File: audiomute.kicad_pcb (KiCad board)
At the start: 2 copper layers, 72.8 x 35.4 mm, 21 parts, among them J1 MJ-3523-SMT, J2 B2B-XH-A_LF__SN_, J3 B2B-XH-A_LF__SN_, J4 MJ-3523-SMT, Q1 MMBT3904, Q2 MMBT3906, Q3 MMBT3904, Q4 MMBT3904

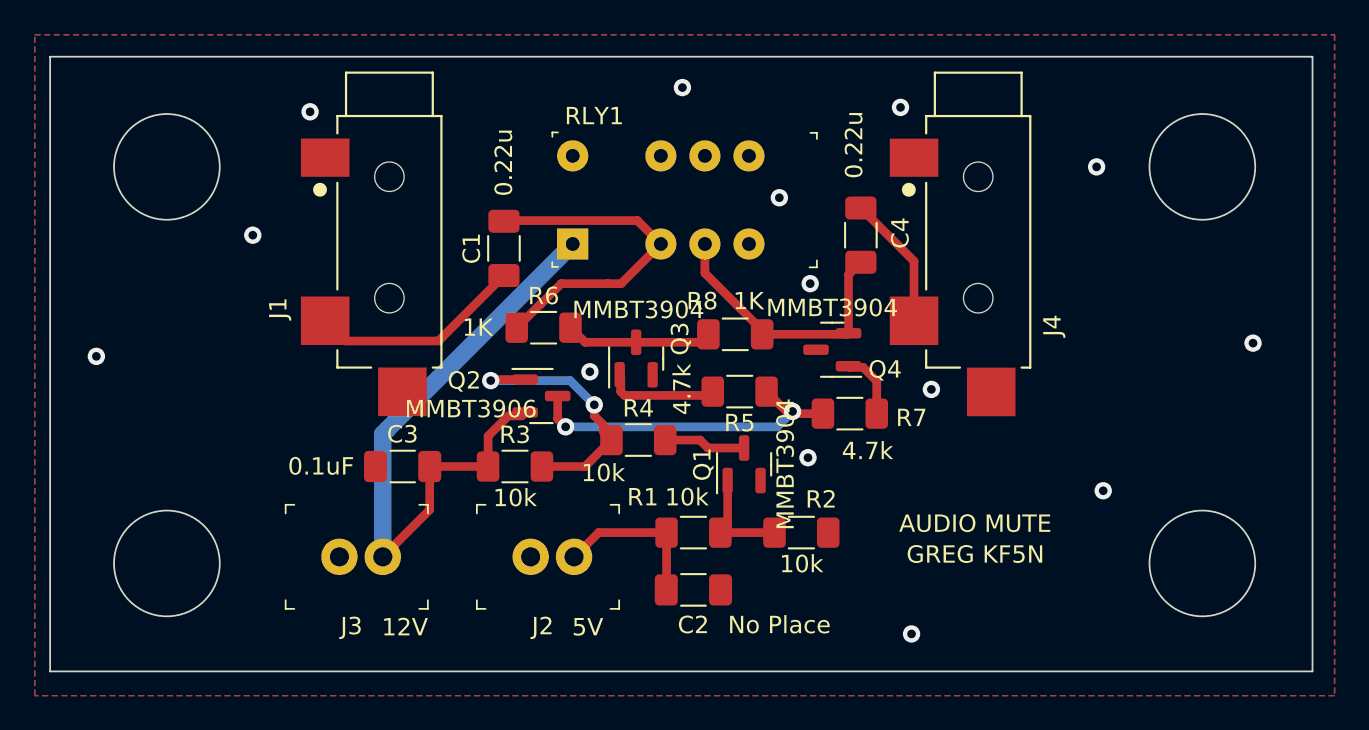
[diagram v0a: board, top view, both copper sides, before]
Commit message: Minor updates to layout and created new gerbers and drills.
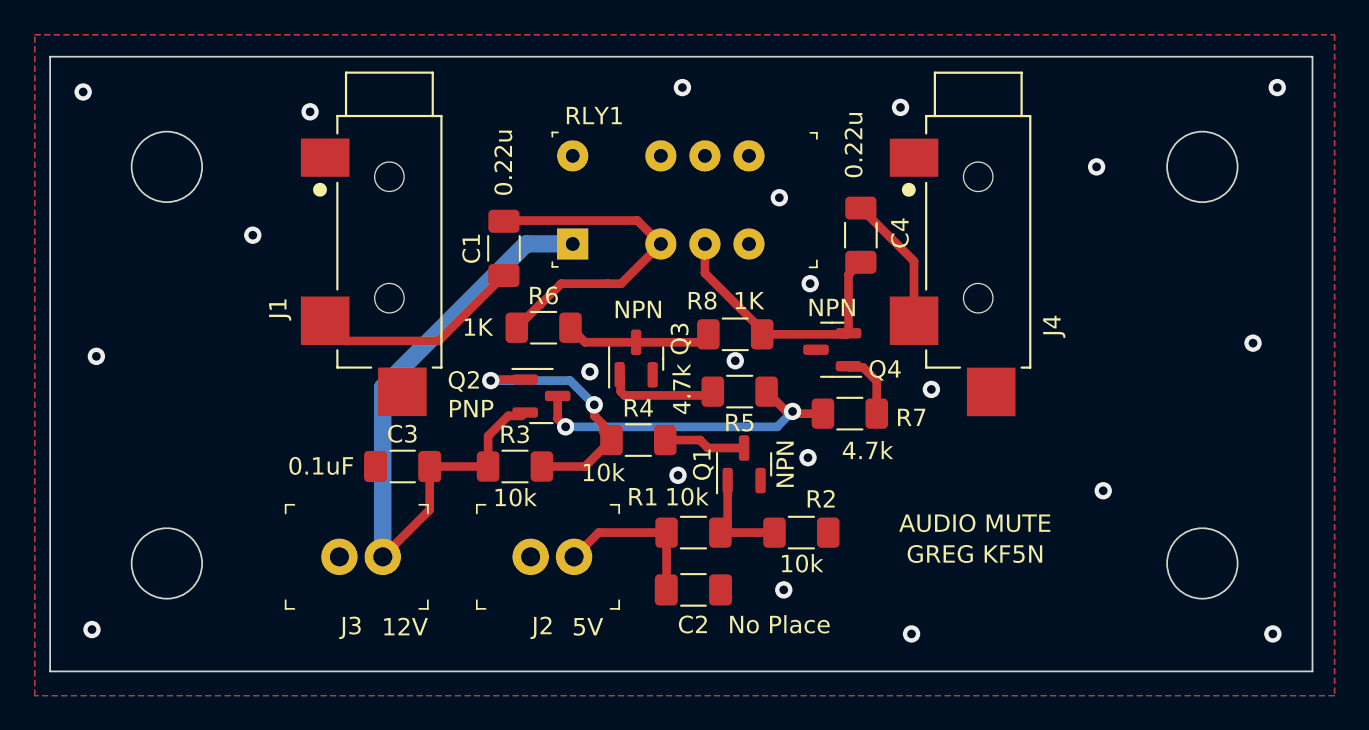
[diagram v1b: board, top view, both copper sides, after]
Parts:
- Q1, Q3, Q4: value MMBT3904 -> NPN
- Q2: value MMBT3906 -> PNP
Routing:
- net Net-(C3-Pad2): track 36.7 -> 38.3 mm
- net GND: vias 14 -> 21
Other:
- outline, holes or cut-outs redrawn
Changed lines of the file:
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@@
       (drillshape 0)
       (scaleselection 1)
-      (outputdirectory "gerber/")
+      (outputdirectory "gerber/Gerbers_May_28_2022/")
     )
   )
@@
       (effects (font (size 1 1) (thickness 0.15)))
     )
-    (fp_text value "MMBT3904" (at 0 2.4 90) (layer "F.SilkS")
+    (fp_text value "NPN" (at 0 2.4 90) (layer "F.SilkS")
       (effects (font (size 1 1) (thickness 0.15)))
     )
@@
       (effects (font (size 1 1) (thickness 0.15)))
     )
-    (fp_text value "MMBT3904" (at 2.794 0.127 180) (layer "F.SilkS")
+    (fp_text value "NPN" (at 2.794 0.127 180) (layer "F.SilkS")
       (effects (font (size 1 1) (thickness 0.15)))
     )
@@
       (effects (font (size 1 1) (thickness 0.15)))
     )
-    (fp_text value "MMBT3906" (at -4.064 0.762) (layer "F.SilkS")
+    (fp_text value "PNP" (at -4.064 0.762) (layer "F.SilkS")
       (effects (font (size 1 1) (thickness 0.15)))
     )
@@
       (effects (font (size 1 1) (thickness 0.15)))
     )
-    (fp_text value "MMBT3904" (at 0 2.4) (layer "F.SilkS")
+    (fp_text value "NPN" (at 0 2.4) (layer "F.SilkS")
       (effects (font (size 1 1) (thickness 0.15)))
     )
@@
     )
   )
+  (gr_circle (center 77.47 78.74) (end 79.502 78.74) (layer "Edge.Cuts") (width 0.1) (fill none))
   (gr_rect (start 70.739 72.39) (end 143.51 107.823) (layer "Edge.Cuts") (width 0.1) (fill none))
-  (gr_circle (center 137.16 101.6) (end 140.208 101.6) (layer "Edge.Cuts") (width 0.1) (fill none))
-  (gr_circle (center 77.47 101.6) (end 80.518 101.6) (layer "Edge.Cuts") (width 0.1) (fill none))
-  (gr_circle (center 77.47 78.74) (end 80.518 78.74) (layer "Edge.Cuts") (width 0.1) (fill none))
-  (gr_circle (center 137.16 78.74) (end 140.208 78.74) (layer "Edge.Cuts") (width 0.1) (fill none))
+  (gr_circle (center 137.16 101.6) (end 139.192 101.6) (layer "Edge.Cuts") (width 0.1) (fill none))
+  (gr_circle (center 137.16 78.74) (end 139.192 78.74) (layer "Edge.Cuts") (width 0.1) (fill none))
+  (gr_circle (center 77.47 101.6) (end 79.502 101.6) (layer "Edge.Cuts") (width 0.1) (fill none))
   (gr_text "GREG KF5N" (at 124.079 101.092) (layer "F.SilkS")
     (effects (font (size 1 1) (thickness 0.15)))
@@
   (segment (start 104.595489 81.835489) (end 96.942011 81.835489) (width 0.5) (layer "F.Cu") (net 2))
   (segment (start 97.637 88.011) (end 98.96152 86.68648) (width 0.5) (layer "F.Cu") (net 2))
+  (via (at 141.478 74.168) (size 1) (drill 0.5) (layers "F.Cu" "B.Cu") (free) (net 3))
+  (via (at 110.236 89.916) (size 1) (drill 0.5) (layers "F.Cu" "B.Cu") (free) (net 3))
   (via (at 101.854 90.551) (size 1) (drill 0.5) (layers "F.Cu" "B.Cu") (free) (net 3))
   (via (at 107.188 74.168) (size 1) (drill 0.5) (layers "F.Cu" "B.Cu") (free) (net 3))
@@
   (via (at 114.554 85.471) (size 1) (drill 0.5) (layers "F.Cu" "B.Cu") (free) (net 3))
   (via (at 112.776 80.518) (size 1) (drill 0.5) (layers "F.Cu" "B.Cu") (free) (net 3))
+  (via (at 106.934 96.52) (size 1) (drill 0.5) (layers "F.Cu" "B.Cu") (free) (net 3))
+  (via (at 73.152 105.41) (size 1) (drill 0.5) (layers "F.Cu" "B.Cu") (free) (net 3))
   (via (at 120.396 105.664) (size 1) (drill 0.5) (layers "F.Cu" "B.Cu") (free) (net 3))
   (via (at 73.406 89.662) (size 1) (drill 0.5) (layers "F.Cu" "B.Cu") (free) (net 3))
   (via (at 114.427 95.504) (size 1) (drill 0.5) (layers "F.Cu" "B.Cu") (free) (net 3))
+  (via (at 141.224 105.664) (size 1) (drill 0.5) (layers "F.Cu" "B.Cu") (free) (net 3))
   (via (at 82.423 82.677) (size 1) (drill 0.5) (layers "F.Cu" "B.Cu") (free) (net 3))
   (via (at 121.539 91.567) (size 1) (drill 0.5) (layers "F.Cu" "B.Cu") (free) (net 3))
   (via (at 131.064 78.74) (size 1) (drill 0.5) (layers "F.Cu" "B.Cu") (free) (net 3))
+  (via (at 113.03 103.124) (size 1) (drill 0.5) (layers "F.Cu" "B.Cu") (free) (net 3))
   (via (at 85.725 75.565) (size 1) (drill 0.5) (layers "F.Cu" "B.Cu") (free) (net 3))
+  (via (at 72.644 74.422) (size 1) (drill 0.5) (layers "F.Cu" "B.Cu") (free) (net 3))
   (via (at 131.445 97.409) (size 1) (drill 0.5) (layers "F.Cu" "B.Cu") (free) (net 3))
   (via (at 140.081 88.9) (size 1) (drill 0.5) (layers "F.Cu" "B.Cu") (free) (net 3))
@@
   (segment (start 95.986 96.012) (end 95.986 94.26) (width 0.5) (layer "F.Cu") (net 5))
   (segment (start 89.911 101.219) (end 89.911 94.139) (width 1) (layer "B.Cu") (net 5))
-  (segment (start 89.911 94.139) (end 90.1835 93.8665) (width 1) (layer "B.Cu") (net 5))
-  (segment (start 90.1835 93.8665) (end 100.865 83.185) (width 1) (layer "B.Cu") (net 5))
+  (segment (start 100.865 83.185) (end 98.171 83.185) (width 1) (layer "B.Cu") (net 5))
+  (segment (start 98.171 83.185) (end 89.911 91.445) (width 1) (layer "B.Cu") (net 5))
+  (segment (start 89.911 91.445) (end 89.911 94.139) (width 1) (layer "B.Cu") (net 5))
   (segment (start 120.54 84.1795) (end 117.475 81.1145) (width 0.5) (layer "F.Cu") (net 6))
   (segment (start 120.54 87.61) (end 120.54 84.1795) (width 0.5) (layer "F.Cu") (net 6))
@@
   (segment (start 116.7005 88.392) (end 116.7615 88.331) (width 0.5) (layer "F.Cu") (net 18))
   (segment (start 111.786 88.164) (end 108.485 84.863) (width 0.5) (layer "F.Cu") (net 18))
+  (zone (net 0) (net_name "") (layer "F.Cu") (name "Q1 keepout") (hatch edge 0.508)
+    (connect_pads (clearance 0))
+    (min_thickness 0.254)
+    (keepout (tracks not_allowed) (vias not_allowed) (pads not_allowed ) (copperpour not_allowed) (footprints allowed))
+    (fill (thermal_gap 0.508) (thermal_bridge_width 0.508))
+    (polygon
+      (pts
+        (xy 110.998 99.06)
+        (xy 110.49 99.06)
+        (xy 110.49 96.266)
+        (xy 110.998 96.266)
+      )
+    )
+  )
+  (zone (net 0) (net_name "") (layer "F.Cu") (name "C3 keepout") (hatch edge 0.508)
+    (connect_pads (clearance 0))
+    (min_thickness 0.254)
+    (keepout (tracks not_allowed) (vias not_allowed) (pads not_allowed ) (copperpour not_allowed) (footprints allowed))
+    (fill (thermal_gap 0.508) (thermal_bridge_width 0.508))
+    (polygon
+      (pts
+        (xy 91.694 97.028)
+        (xy 90.424 97.028)
+        (xy 90.424 95.25)
+        (xy 91.694 95.25)
+      )
+    )
+  )
+  (zone (net 0) (net_name "") (layer "F.Cu") (name "R2 keepout") (hatch edge 0.508)
+    (connect_pads (clearance 0))
+    (min_thickness 0.254)
+    (keepout (tracks not_allowed) (vias not_allowed) (pads not_allowed ) (copperpour not_allowed) (footprints allowed))
+    (fill (thermal_gap 0.508) (thermal_bridge_width 0.508))
+    (polygon
+      (pts
+        (xy 114.808 100.584)
+        (xy 113.284 100.584)
+        (xy 113.284 99.06)
+        (xy 114.808 99.06)
+      )
+    )
+  )
+  (zone (net 0) (net_name "") (layer "F.Cu") (name "C2 keepout") (hatch edge 0.508)
+    (connect_pads (clearance 0))
+    (min_thickness 0.254)
+    (keepout (tracks not_allowed) (vias not_allowed) (pads not_allowed ) (copperpour not_allowed) (footprints allowed))
+    (fill (thermal_gap 0.508) (thermal_bridge_width 0.508))
+    (polygon
+      (pts
+        (xy 108.458 103.886)
+        (xy 107.188 103.886)
+        (xy 107.188 102.362)
+        (xy 108.458 102.362)
+      )
+    )
+  )
   (zone (net 3) (net_name "GND") (layer "F.Cu") (hatch edge 0.508)
     (connect_pads (clearance 0.508))

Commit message: Finished version 1.0.  Ready to release PCB.
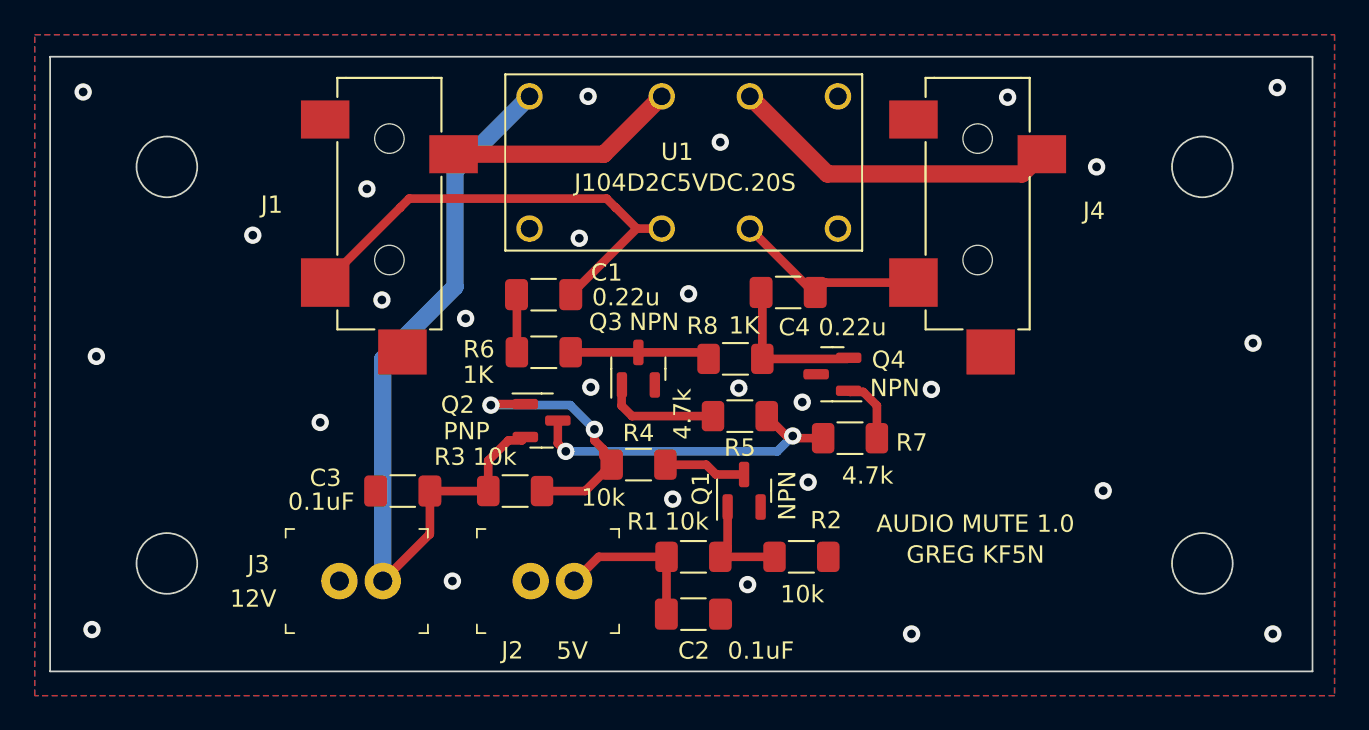
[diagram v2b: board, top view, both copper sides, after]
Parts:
- removed RLY1: EC2-12NU, digikey-footprints:Relay_THT_EC2
- added U1: J104D2C5VDC.20S, Relay_DPDT_GP:J104D2C5VDC.20S, F.Cu at (98.4, 82.3)
- C2: value No Place -> 0.1uF
- J1, J4: value MJ-3523-SMT -> SJ-3524-SMT; footprint MJ-3523-SMT:CUI_MJ-3523-SMT -> Stereo_Jack_SMT:CUI_SJ-3524-SMT
- moved J4 5.95 mm to (124.2, 77.1), turned to -90 degrees
- moved J1 5.95 mm to (90.3, 77.1), turned to -90 degrees
- moved C4 5.34 mm to (113.3, 86.0), turned to 0 degrees
- moved C1 3.51 mm to (99.2, 86.1), turned to 180 degrees
- moved Q1 1.52 mm to (110.7, 97.4)
- moved C3 1.41 mm to (91.1, 97.4)
- moved Q2 1.41 mm to (99.1, 93.4)
- moved R3 1.41 mm to (97.5, 97.4)
- moved R4 1.41 mm to (104.7, 95.9)
- moved R6 1.41 mm to (99.2, 89.4)
- moved R7 1.41 mm to (116.8, 94.4)
- moved R8 1.41 mm to (110.2, 89.8)
- moved Q4 1.41 mm to (115.8, 90.7)
- moved R5 1.41 mm to (110.5, 93.1)
- moved C2 1.40 mm to (107.8, 104.5)
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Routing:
- net Net-(J4-Pad3): track 0.00 -> 19.2 mm
- net Net-(C1-Pad2): track 19.9 -> 3.33 mm
- net Net-(C1-Pad1): track 12.3 -> 27.5 mm
- net Net-(J1-Pad3): track 0.00 -> 13.4 mm
- net Net-(C3-Pad2): track 38.3 -> 45.6 mm
- net Net-(C4-Pad1): track 16.0 -> 8.86 mm
- net Net-(C4-Pad2): track 7.77 -> 11.2 mm
- net GND: vias 21 -> 27
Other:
- outline, holes or cut-outs redrawn
- board text added: "AUDIO MUTE 1.0"
- board text removed: "AUDIO MUTE"

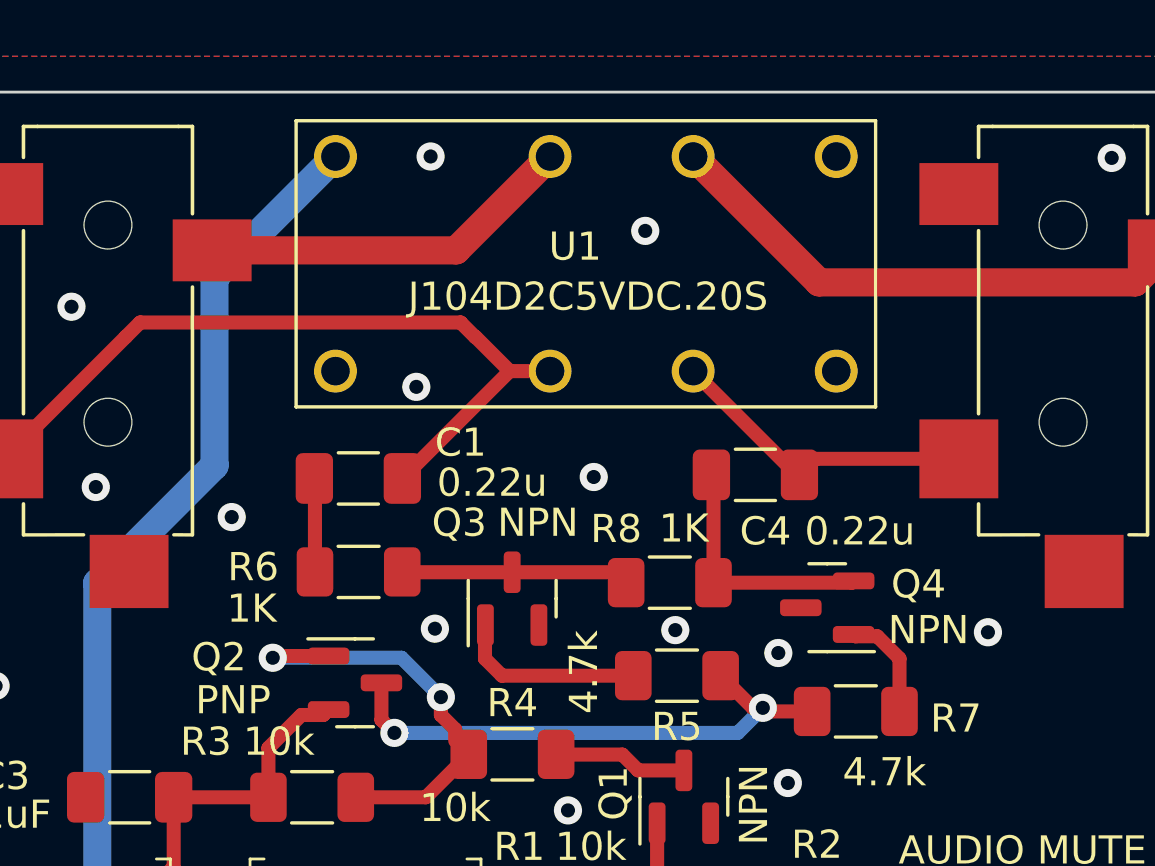
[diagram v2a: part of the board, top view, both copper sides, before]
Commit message: Revised board uses larger relay, and has differential input and output.
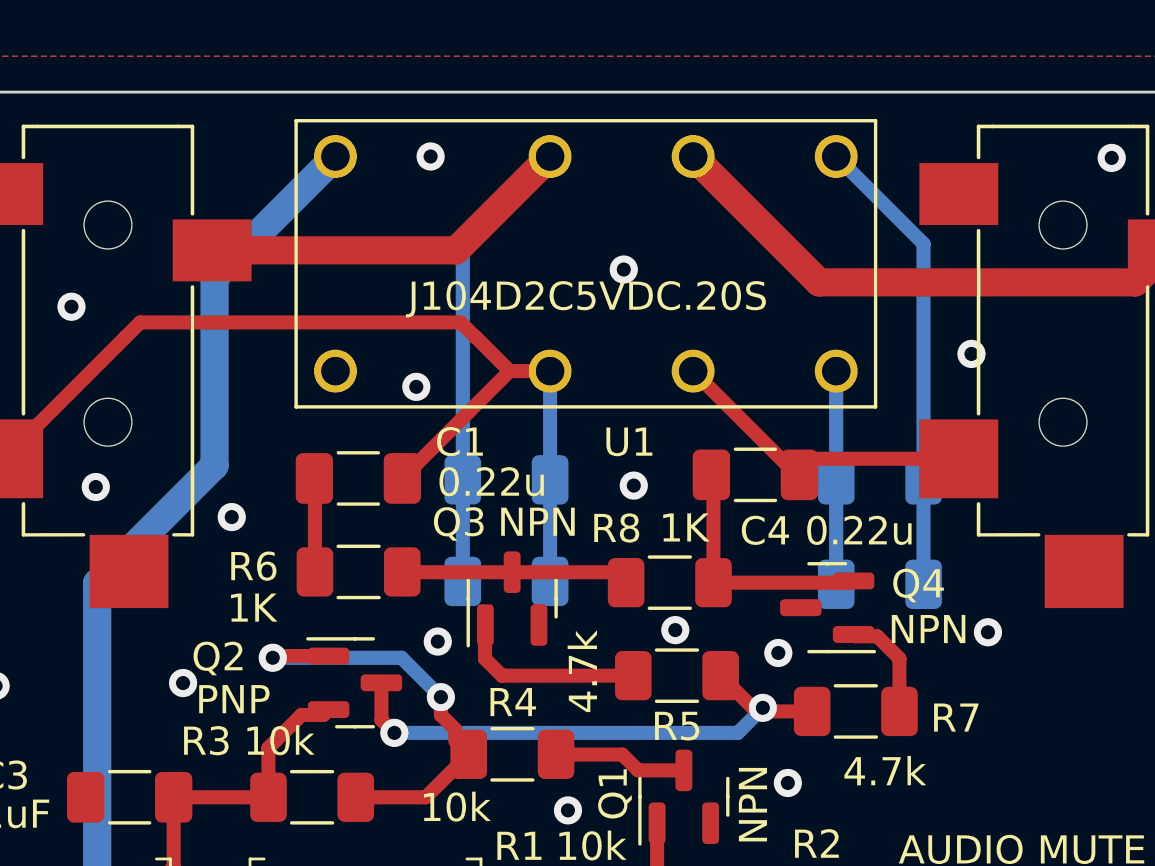
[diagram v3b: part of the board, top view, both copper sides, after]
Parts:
- added R10: 1.0k, Resistor_SMD:R_1206_3216Metric_Pad1.30x1.75mm_HandSolder, B.Cu at (104.4, 89.8)
- added R11: 1K, Resistor_SMD:R_1206_3216Metric_Pad1.30x1.75mm_HandSolder, B.Cu at (117.7, 86.2)
- added R12: 1K, Resistor_SMD:R_1206_3216Metric_Pad1.30x1.75mm_HandSolder, B.Cu at (117.7, 89.9)
- added R9: 1.0k, Resistor_SMD:R_1206_3216Metric_Pad1.30x1.75mm_HandSolder, B.Cu at (104.4, 86.2)
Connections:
- U1 pad 4: unconnected-(U1-Pad4) -> Net-(U1-Pad4)
- U1 pad 5: unconnected-(U1-Pad5) -> Net-(U1-Pad5)
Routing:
- net Net-(U1-Pad5): track 0.00 -> 16.5 mm
- net Net-(J1-Pad3): track 13.4 -> 29.7 mm
- net Net-(U1-Pad4): track 0.00 -> 7.57 mm
- net Net-(C1-Pad1): track 27.5 -> 35.0 mm
- net GND: vias 27 -> 29
